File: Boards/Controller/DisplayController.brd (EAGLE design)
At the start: 54 x 39 mm, 46 parts, among them J1 USB0001LF, J3 AVR_SPI_PRG_62X3_LOCK, Q1 BSS138, U1 MCP1703CB, U100 MCP73831, U101 MAX1797, U2 FT232RQ, U3 ATMEGA328P-MU, U5 MAX1704X, X2 CRYSTAL7A-20.000MAAJ-T

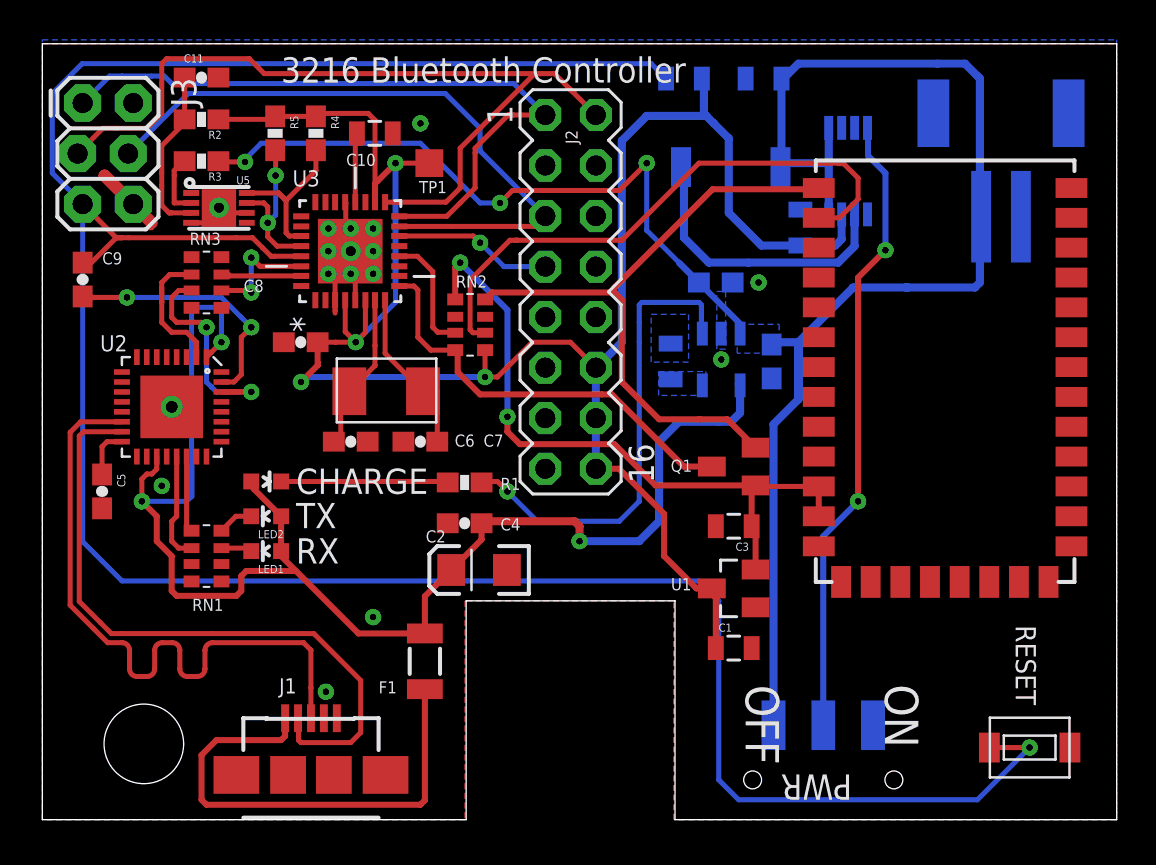
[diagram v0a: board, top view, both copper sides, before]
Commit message: Increased +5V trace width to 0.6096mm cleaned up traces removed 3 vias changed to eagle 6.1.0
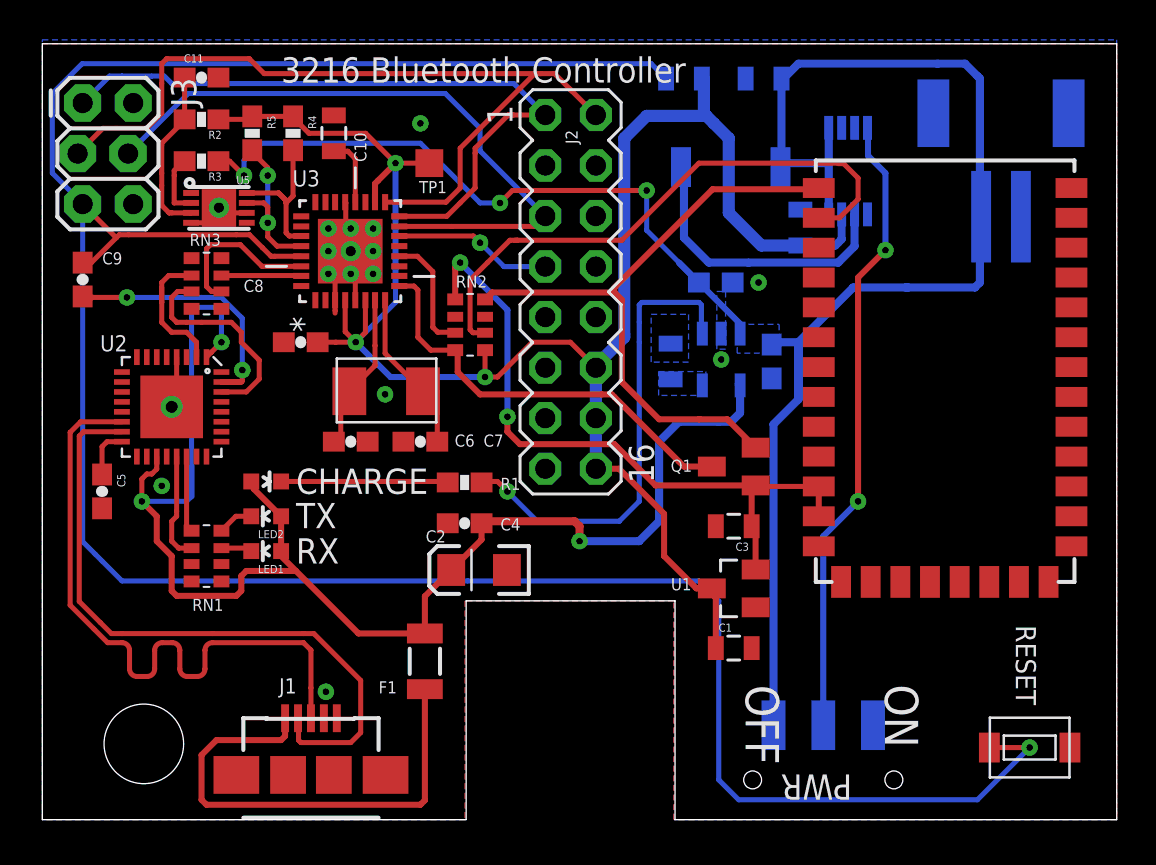
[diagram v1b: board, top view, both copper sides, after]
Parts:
- moved C10 2.06 mm to (14.7, 34.5), turned to 90 degrees
- moved R4 1.15 mm to (12.6, 34.5)
- moved R5 1.15 mm to (10.6, 34.5)
- moved RN3 0.05 mm to (8.25, 26.9)
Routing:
- net VCC: track 101.6 -> 96.2 mm, vias 4 -> 3
- net GND: track 17.9 -> 15.0 mm
- net N$12: track 13.3 -> 15.6 mm
- net N$15: track 5.98 -> 8.05 mm, vias 2 -> 0
- net RX: track 11.8 -> 10.8 mm, vias 2 -> 0
- net PACK+: track 107.0 -> 106.2 mm
- net N$1: track 3.92 -> 3.42 mm

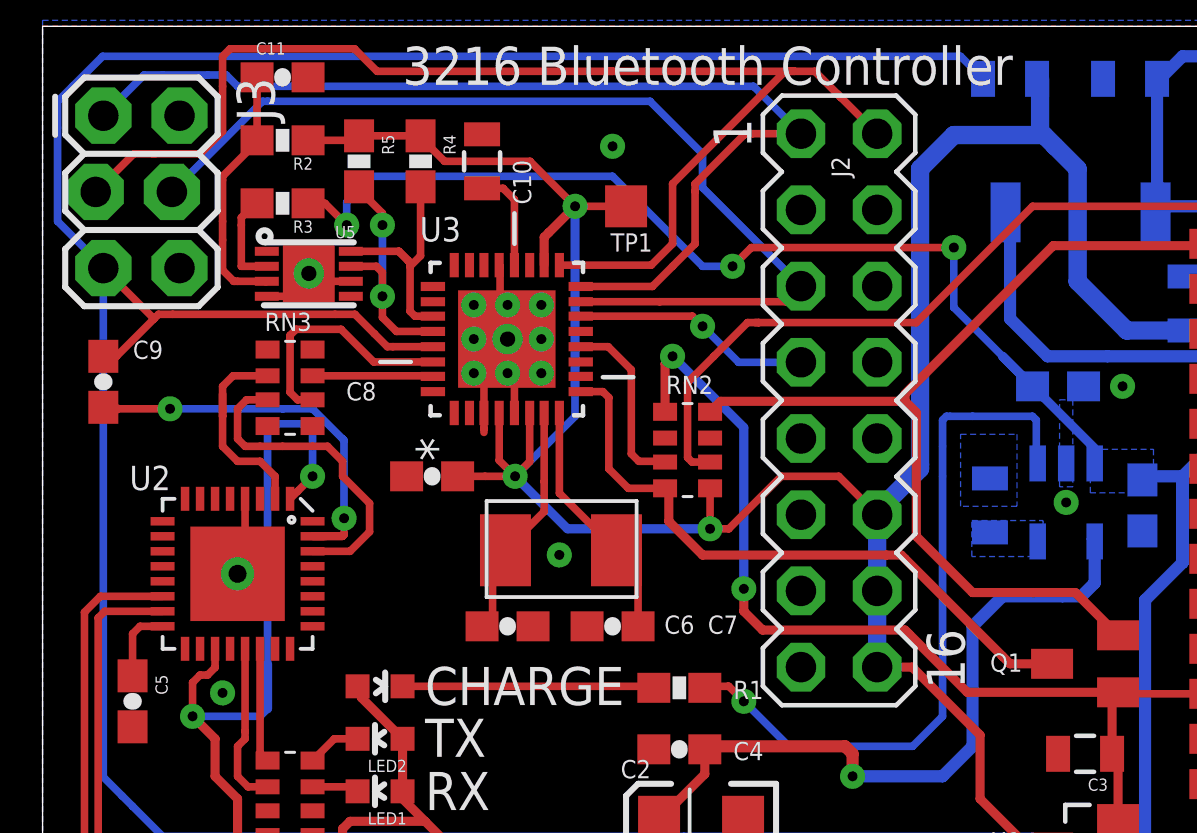
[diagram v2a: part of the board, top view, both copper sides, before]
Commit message: Added Thermistor to determine board temperature Cleaned up thermal vias and traces under ICs
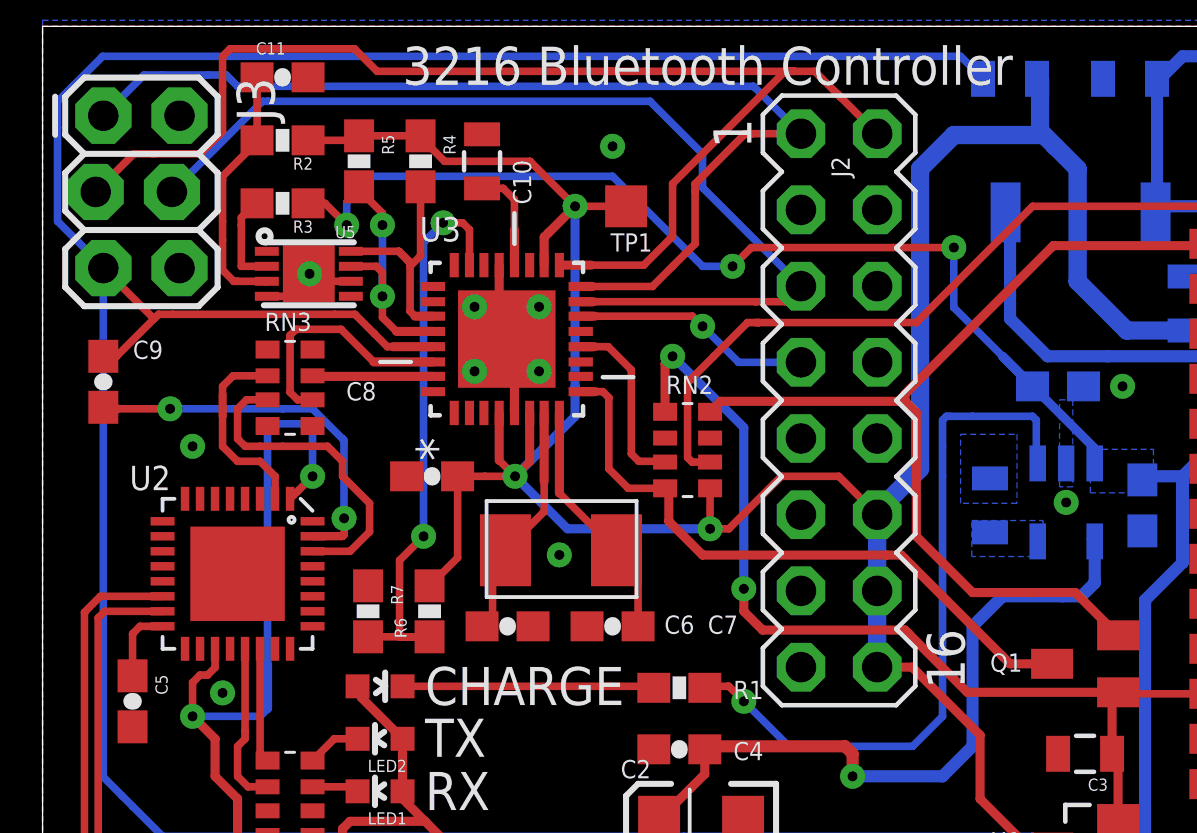
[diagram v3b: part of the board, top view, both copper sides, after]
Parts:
- added R6: 10K NTC, SparkFun:0603-RES
- added R7: 10K, SparkFun:0603-RES
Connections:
- new net N$18: R6.1, R7.2, U3.23
- net GND: now also R7.1
- net VCC: now also R6.2
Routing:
- net N$18: track 0.00 -> 20.7 mm, vias 0 -> 2
- net GND: track 15.0 -> 9.55 mm, vias 17 -> 12
- net VCC: track 96.2 -> 100.3 mm

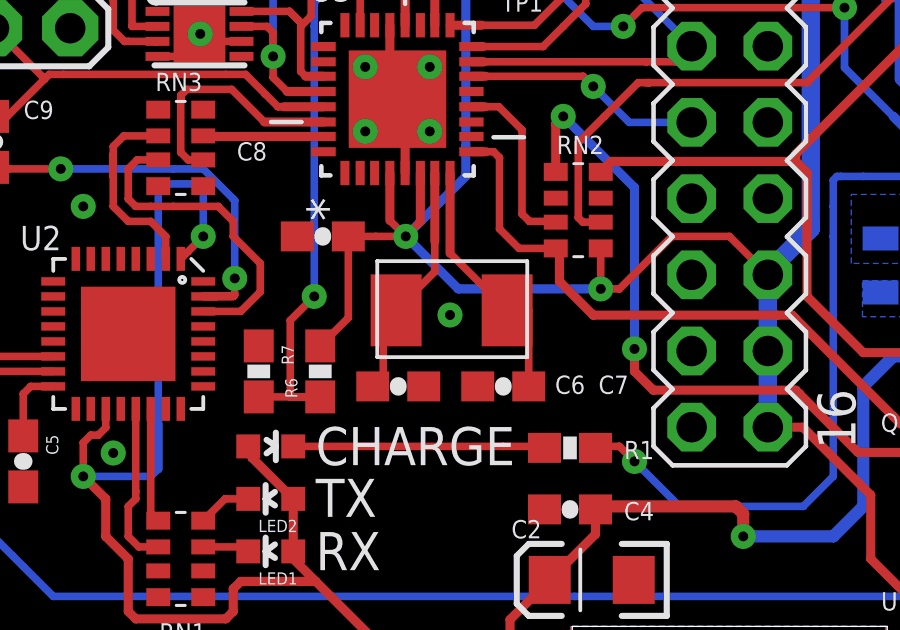
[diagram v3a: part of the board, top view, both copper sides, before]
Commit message: Removed extra ground via from under crystal
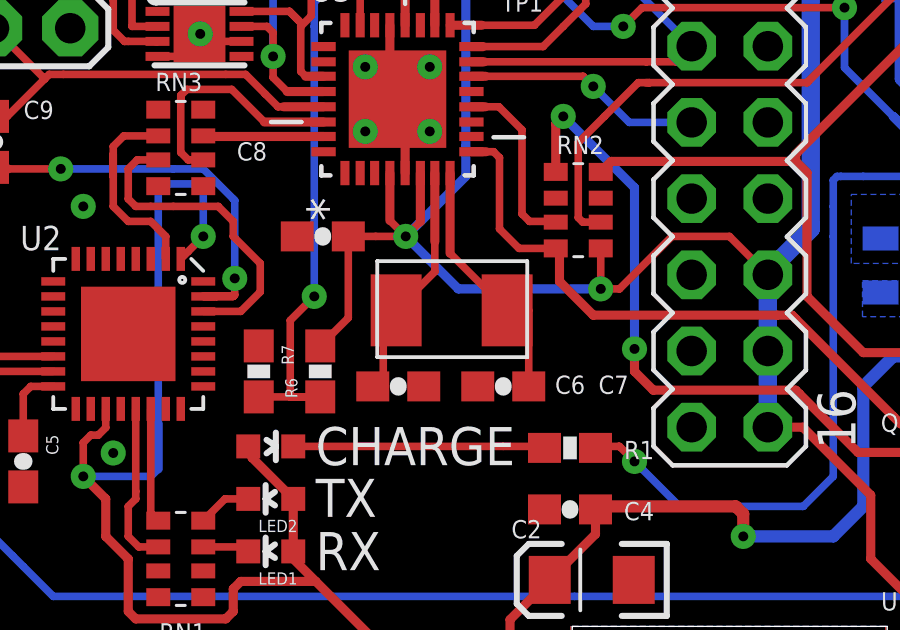
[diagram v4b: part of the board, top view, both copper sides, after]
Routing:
- net GND: vias 12 -> 11
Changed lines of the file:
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@@
 <wire x1="7.47500625" y1="30.0000125" x2="8.87500625" y2="30.0000125" width="0.254" layer="1"/>
 <wire x1="8.87500625" y1="30.0000125" x2="8.87500625" y2="30.7500125" width="0.254" layer="1"/>
-<via x="17.225" y="21.38" extent="1-16" drill="0.3302"/>
 <via x="19" y="35" extent="1-16" drill="0.3302"/>
 <via x="36" y="27" extent="1-16" drill="0.3302" diameter="0.8382"/>

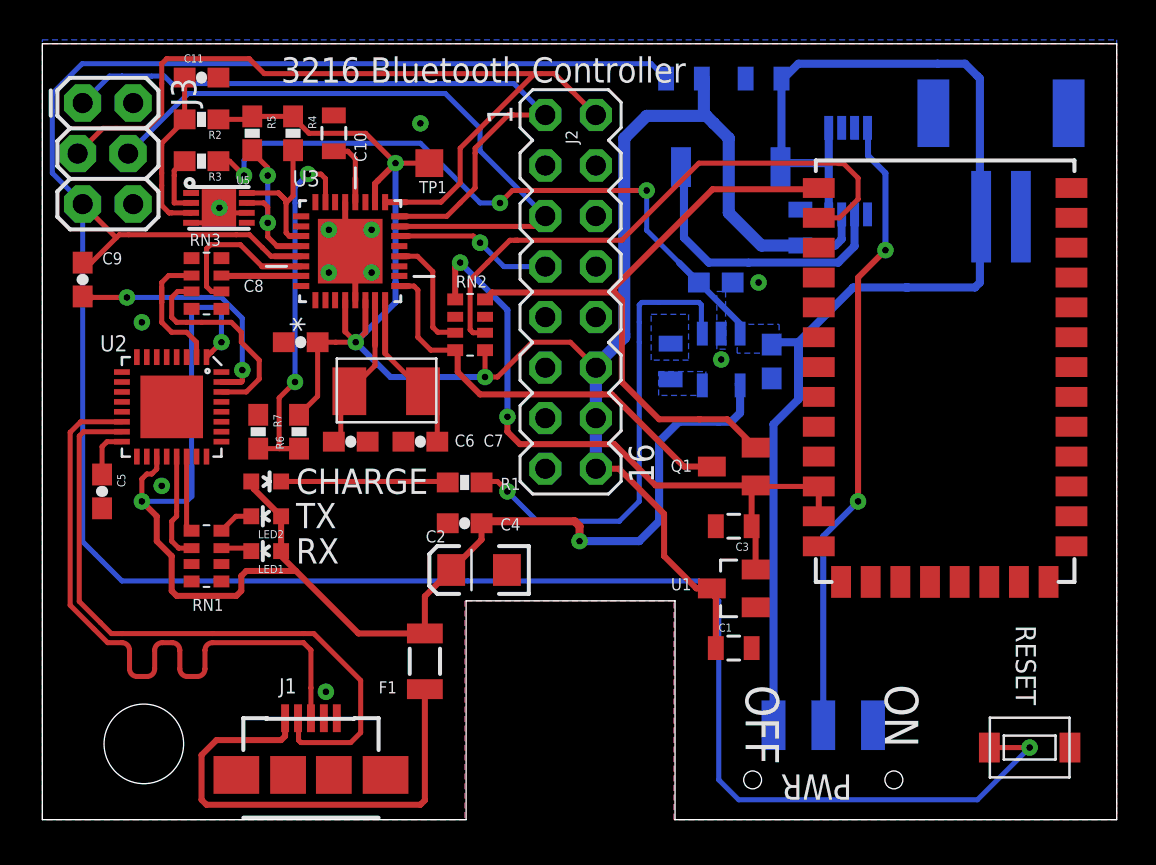
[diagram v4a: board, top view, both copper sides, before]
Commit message: cleaned up controller traces replaced power switch with new part from sparkfun (deprecated old switch) removed thermistor (nice to have but not really needed for now)
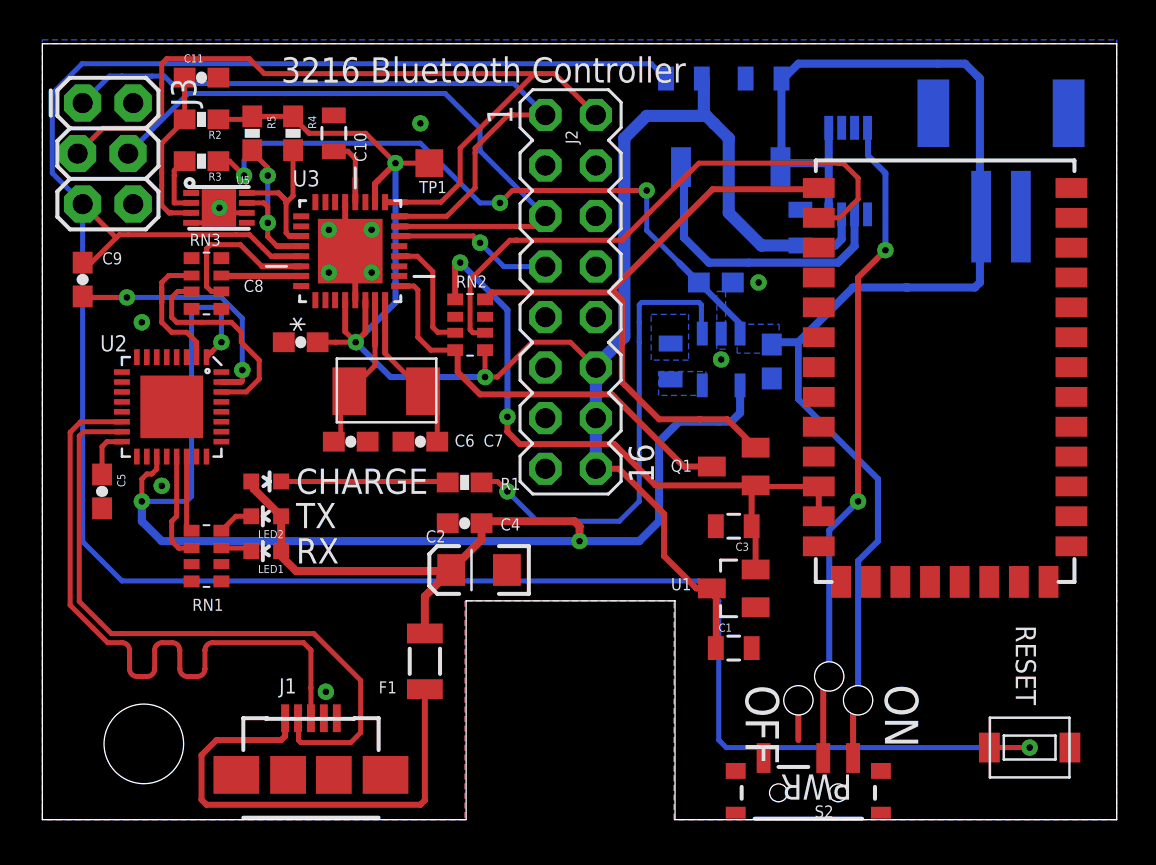
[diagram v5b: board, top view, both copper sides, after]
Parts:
- removed R6: 10K NTC, SparkFun:0603-RES
- removed R7: 10K, SparkFun:0603-RES
- removed S100: (no value), SparkFun:SWITCH-SPDT-SMD
- added JP1, JP2, JP3: M01POGOPIN_HOLE_0.58, SparkFun-Connectors:1X01_POGOPIN_HOLE_0.58
- added S2: (no value), SparkFun-Electromechanical:SWITCH-SPST-SMD-A
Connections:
- removed net N$18: R6.1, R7.2, U3.23
- net GND: now also JP1.1, S2.3; no longer R7.1, S100.3
- net PACK+: now also JP3.1, S2.1; no longer S100.1
- net SHDN: now also JP2.1, S2.2; no longer S100.2
- net VCC: no longer R6.2
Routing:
- net N$18: track 20.7 -> 0.00 mm, vias 2 -> 0
- net USB5V: track 72.7 -> 83.7 mm
- net VCC: track 100.3 -> 96.2 mm
- net RESET: track 130.8 -> 127.4 mm
- net GND: track 9.55 -> 11.5 mm
- net SHDN: track 31.7 -> 33.3 mm

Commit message: moved Power supplies to top side cleaned up traces moved reset switch near display connector Added various Newark part numbers to board parts
Signed-off-by: evanrich <erichardson@savi.com>
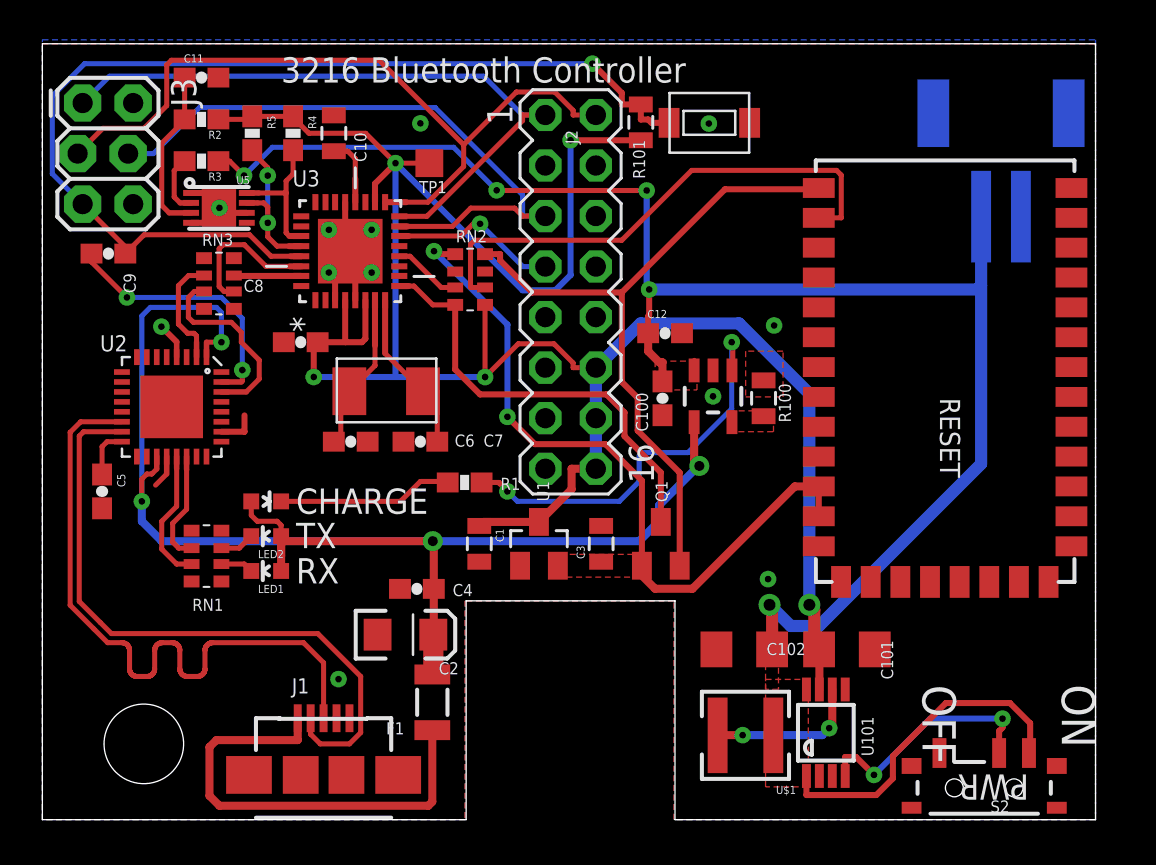
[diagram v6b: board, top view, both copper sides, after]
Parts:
- removed JP1, JP2, JP3: M01POGOPIN_HOLE_0.58, SparkFun-Connectors:1X01_POGOPIN_HOLE_0.58
- removed L100: 22uH, MyParts:SD53
- added U$1: IFSC1515AHER220M01, MyParts:IFSC
- C101, C102: device SparkFun:0805 -> SparkFun:1206
- moved S1 35.3 mm to (33.5, 35.0)
- moved C102 28.7 mm to (35.3, 8.56), flipped to the top, turned to 180 degrees
- moved U101 28.3 mm to (39.4, 4.37), flipped to the top, turned to 0 degrees
- moved C101 21.3 mm to (40.4, 8.56), flipped to the top, turned to 0 degrees
- moved C1 13.8 mm to (22.0, 13.9), turned to 270 degrees
- moved U1 10.0 mm to (25.0, 13.9), turned to 0 degrees
- moved S2 8.84 mm to (47.3, 1.60)
- moved C3 6.72 mm to (28.1, 13.9), turned to 90 degrees
- moved C100 5.79 mm to (31.2, 21.2), flipped to the top
- moved Q1 5.34 mm to (31.1, 13.9), turned to 0 degrees
- moved R100 5.02 mm to (36.2, 21.2), flipped to the top
- moved C2 4.92 mm to (18.2, 9.30), turned to 0 degrees
- moved C4 4.08 mm to (18.8, 11.6)
- moved C12 3.61 mm to (31.3, 24.4), flipped to the top, turned to 0 degrees
- moved R101 3.09 mm to (30.1, 35.0), flipped to the top, turned to 270 degrees
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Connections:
- net GND: no longer JP1.1
- net N$10: now also RN1.7; no longer RN1.8
- net N$24: now also U$1.2; no longer L100.P$2
- net N$3: now also RN1.2; no longer RN1.1
- net N$4: now also RN1.3; no longer RN1.2
- net N$6: now also RN1.6; no longer RN1.7
- net PACK+: now also U$1.1; no longer JP3.1, L100.P$1
- net SHDN: no longer JP2.1
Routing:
- net RESET: track 127.4 -> 52.8 mm
- net SHDN: track 33.3 -> 12.4 mm
- net VCC: track 96.2 -> 116.2 mm, vias 3 -> 5
- net USB5V: track 83.7 -> 72.9 mm, vias 3 -> 4
- net PACK+: track 106.6 -> 97.3 mm, vias 3 -> 5
- net N$24: track 15.1 -> 7.77 mm, vias 0 -> 2
- net GND: track 11.5 -> 18.2 mm, vias 11 -> 12
- net SCK: track 42.6 -> 38.5 mm
- net N$5: track 23.9 -> 20.6 mm, vias 1 -> 2
- net D8: track 6.52 -> 3.46 mm
- net 3V3TX: track 32.2 -> 34.9 mm
- net 3V3RX: track 29.2 -> 26.5 mm
- net N$12: track 15.6 -> 13.4 mm
- net +3V3: track 34.1 -> 36.1 mm
- net N$3: track 3.83 -> 5.66 mm
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- added copper zone on layer 1, net +3V3
- added copper zone on layer 1, net N$21
- added copper zone on layer 1, net PACK+
- removed copper zone on layer 16, net N$21
- removed copper zone on layer 16, net PACK+
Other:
- board size 54 x 39 mm -> 52.9 x 39 mm

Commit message: added Rev Number (SVN 123) cosmetics
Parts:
- J100: value (none) -> 38K8067
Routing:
- net PACK+: track 97.3 -> 94.5 mm
- net RESET: track 52.8 -> 55.0 mm
- net SHDN: track 12.4 -> 10.5 mm, vias 2 -> 0
- net N$12: track 13.4 -> 14.2 mm
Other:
- board text added: "Rev. 123"
